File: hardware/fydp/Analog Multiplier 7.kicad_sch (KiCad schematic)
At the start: 21 parts, among them J8 Conn_01x02_Pin, U1 LTC2630ISC6-LZ8-TRMPBF, U4 LTC2630ISC6-LZ8-TRMPBF, U5 SN74LVC1G3157DCKR, U6 AD633ARZ-R7

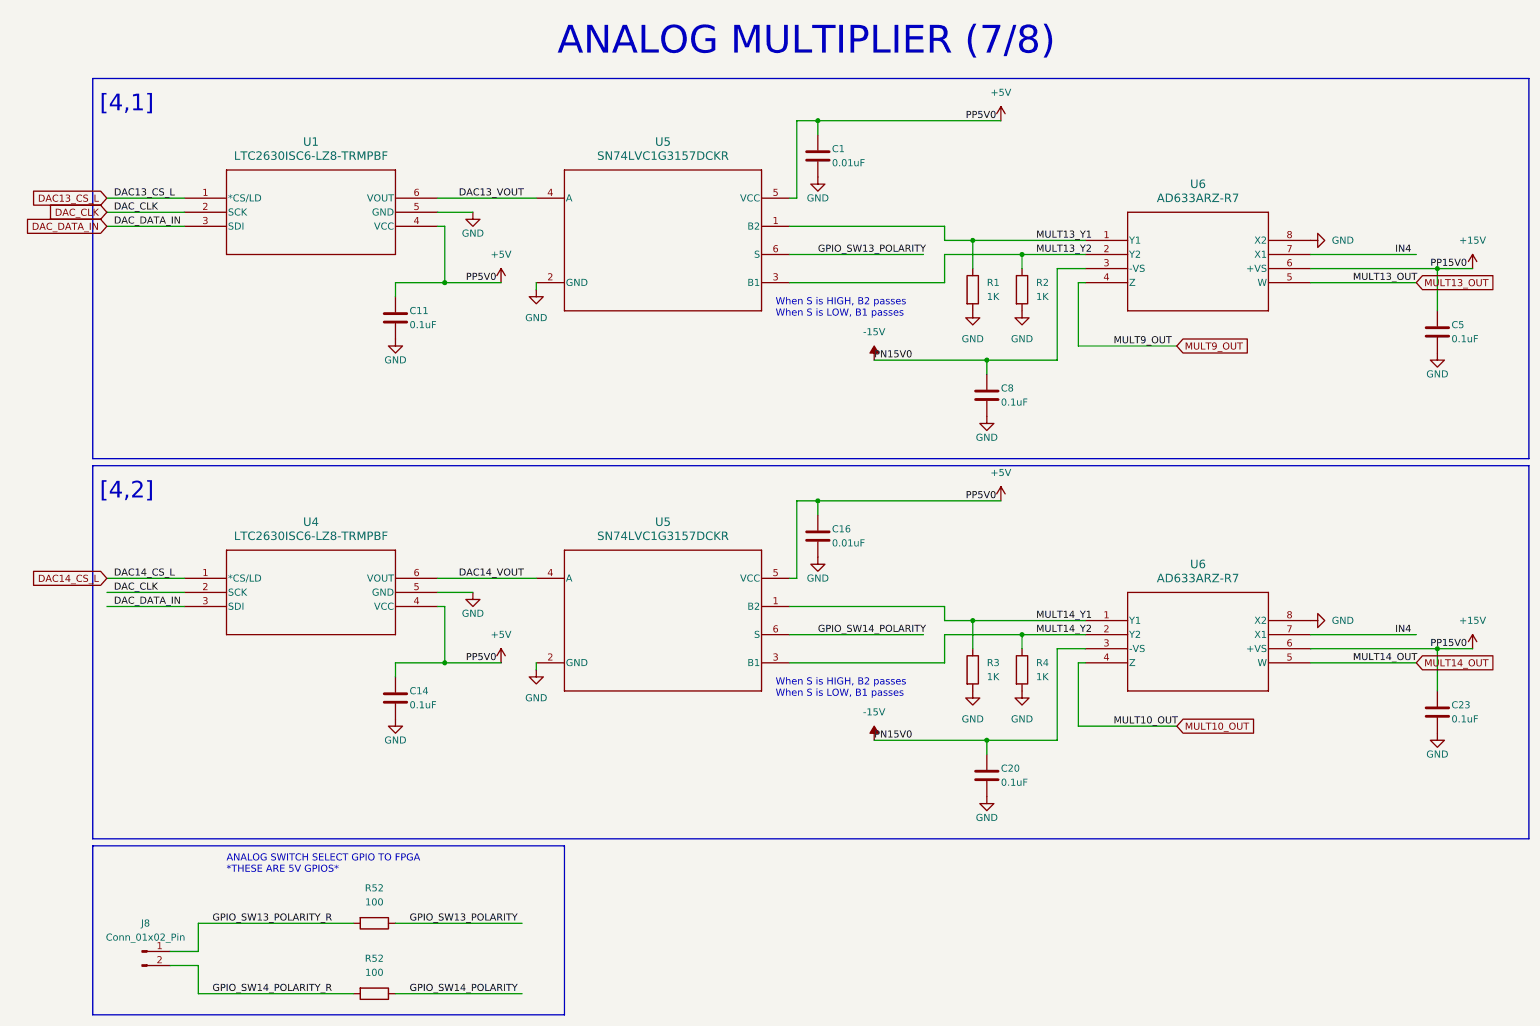
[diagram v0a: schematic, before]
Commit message: Remove 2 channels of multiplier and change ADC
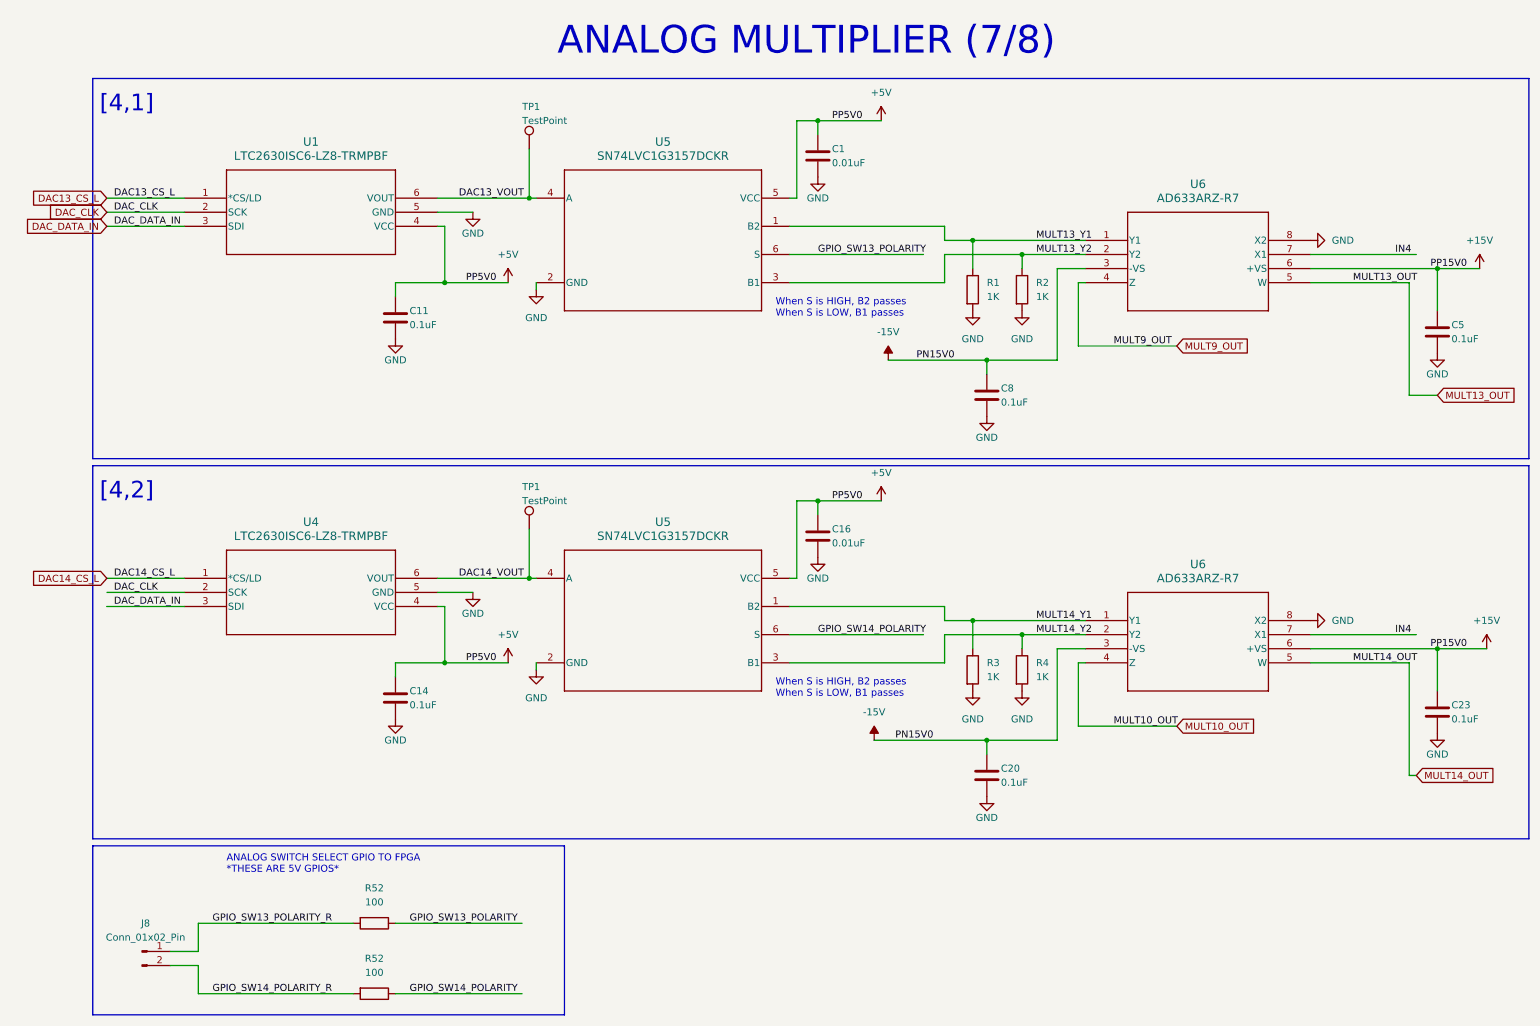
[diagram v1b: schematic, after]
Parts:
- added TP1 (x2): TestPoint, TestPoint:TestPoint_Pad_1.0x1.0mm, symbol Connector:TestPoint
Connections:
- net DAC13_VOUT: now also TP1.1
- net DAC14_VOUT: now also TP1.1

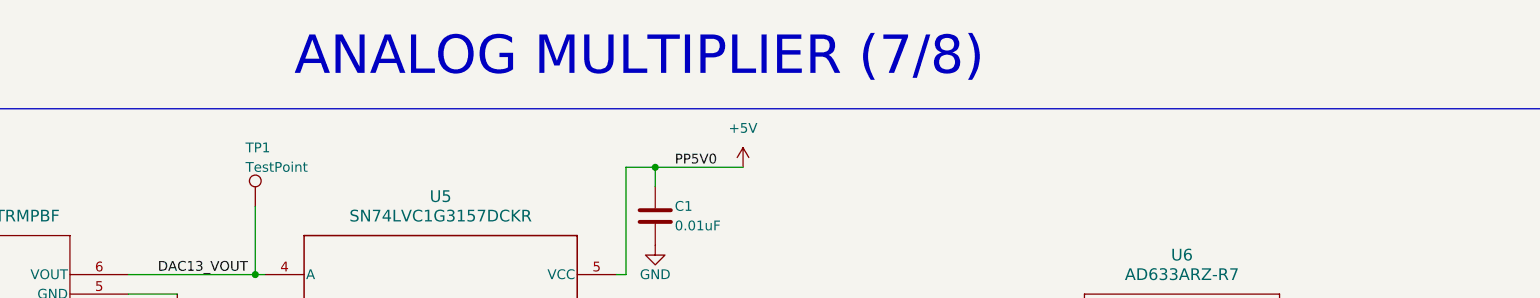
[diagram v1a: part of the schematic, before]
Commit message: Edit schematic titles
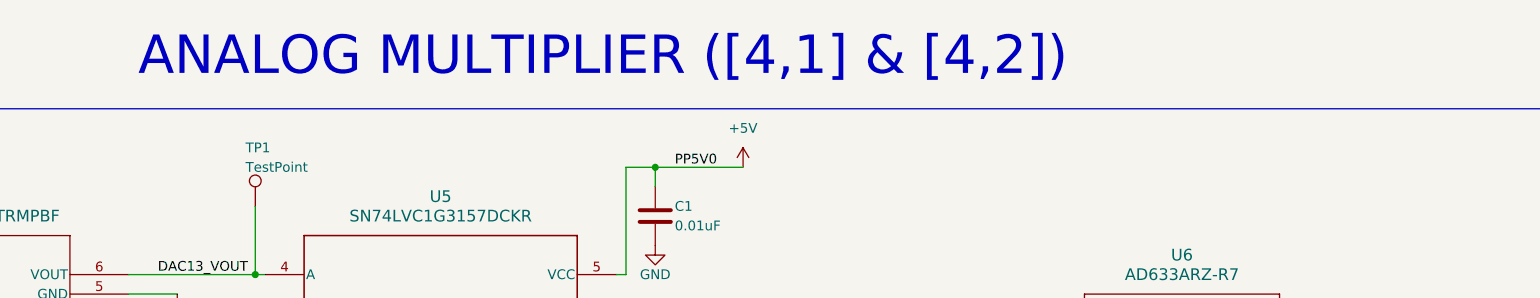
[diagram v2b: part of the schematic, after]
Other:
- note added: "ANALOG MULTIPLIER ([4,1] & [4,2])"
- note removed: "ANALOG MULTIPLIER (7/8)"
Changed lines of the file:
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@@
     (effects (font (size 1.27 1.27)) (justify left bottom))
   )
-  (text "ANALOG MULTIPLIER (7/8)" (at 102.87 22.86 0)
+  (text "ANALOG MULTIPLIER ([4,1] & [4,2])" (at 82.55 22.86 0)
     (effects (font (size 5 5)) (justify left bottom))
   )
